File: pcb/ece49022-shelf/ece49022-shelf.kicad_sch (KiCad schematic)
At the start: 5 parts, among them J2 Conn_01x16_Pin, J3 Conn_01x04_Pin, J6 Conn_01x02_Pin, J7 Conn_01x02_Pin

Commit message: updated footprints, pcb
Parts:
- R11: footprint (none) -> Resistor_SMD:R_0402_1005Metric
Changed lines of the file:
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@@
 			)
 		)
-		(property "Footprint" ""
+		(property "Footprint" "Resistor_SMD:R_0402_1005Metric"
 			(at 179.07 105.41 0)
 			(effects

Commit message: stuff
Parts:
- added H1, H2, H3, H4: MountingHole, MountingHole:MountingHole_2.7mm_M2.5, symbol Mechanical:MountingHole
- R11: footprint Resistor_SMD:R_0402_1005Metric -> Resistor_SMD:R_0805_2012Metric_Pad1.20x1.40mm_HandSolder

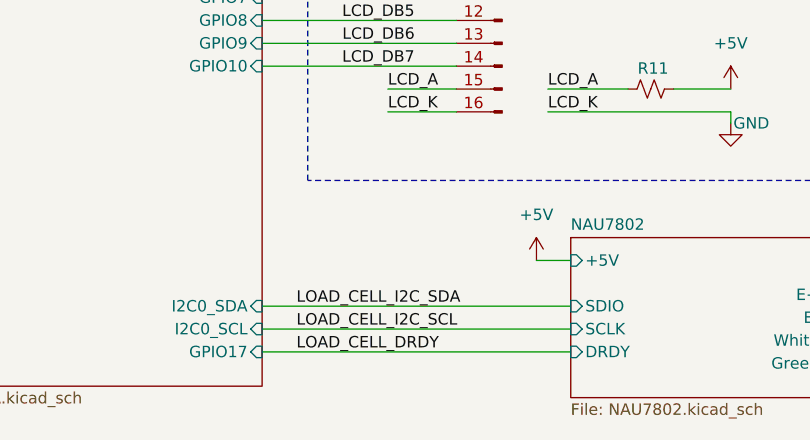
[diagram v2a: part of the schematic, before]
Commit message: edited nau7802 schem and changed pins for layout reasons
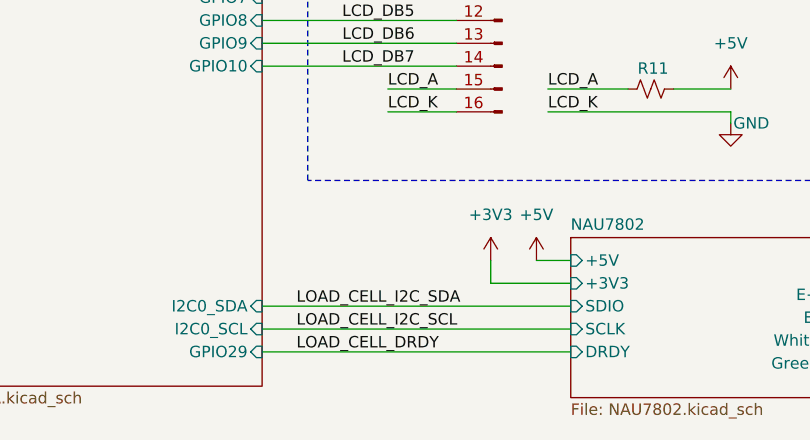
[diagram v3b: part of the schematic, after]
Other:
- sheet NAU7802 ports: added +3V3; removed none
- sheet RP2350A ports: added GPIO29; removed GPIO17
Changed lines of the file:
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@@
+	(wire
+		(pts
+			(xy 170.18 127) (xy 161.29 127)
+		)
+		(stroke
+			(width 0)
+			(type default)
+		)
+	)
 	(wire
 		(pts
@@
 		(pts
 			(xy 167.64 105.41) (xy 176.53 105.41)
+		)
+		(stroke
+			(width 0)
+			(type default)
+		)
+	)
+	(wire
+		(pts
+			(xy 161.29 124.46) (xy 161.29 127)
 		)
 		(stroke
@@
 	)
 	(symbol
+		(lib_id "power:+3V3")
+		(at 161.29 124.46 0)
+		(unit 1)
+		(exclude_from_sim no)
+		(in_bom yes)
+		(on_board yes)
+		(dnp no)
+		(fields_autoplaced yes)
+		(property "Reference" "#PWR02"
+			(at 161.29 128.27 0)
+			(effects
+				(font
+					(size 1.27 1.27)
+				)
+				(hide yes)
+			)
+		)
+		(property "Value" "+3V3"
+			(at 161.29 119.38 0)
+			(effects
+				(font
+					(size 1.27 1.27)
+				)
+			)
+		)
+		(property "Footprint" ""
+			(at 161.29 124.46 0)
+			(effects
+				(font
+					(size 1.27 1.27)
+				)
+				(hide yes)
+			)
+		)
+		(property "Datasheet" ""
+			(at 161.29 124.46 0)
+			(effects
+				(font
+					(size 1.27 1.27)
+				)
+				(hide yes)
+			)
+		)
+		(property "Description" "Power symbol creates a global label with name \"+3V3\""
+			(at 161.29 124.46 0)
+			(effects
+				(font
+					(size 1.27 1.27)
+				)
+				(hide yes)
+			)
+		)
+		(pin "1"
+		)
+		(instances
+			(project ""
+				(path "/cb6cb1b4-c151-4aa2-8cd7-5430288cfa02"
+					(reference "#PWR02")
+					(unit 1)
+				)
+			)
+		)
+	)
+	(symbol
 		(lib_id "Connector:Conn_01x02_Pin")
 		(at 35.56 129.54 0)
@@
 			)
 		)
-		(pin "GPIO17" input
-			(at 135.89 134.62 0)
-			(effects
-				(font
-					(size 1.27 1.27)
-				)
-				(justify right)
-			)
-		)
 		(pin "+3V3" input
 			(at 95.25 77.47 180)
@@
 				)
 				(justify left)
+			)
+		)
+		(pin "GPIO29" input
+			(at 135.89 134.62 0)
+			(effects
+				(font
+					(size 1.27 1.27)
+				)
+				(justify right)
 			)
 		)
@@
 			(effects
 				(font
+					(size 1.27 1.27)
+				)
+				(justify left)
+			)
+		)
+		(pin "+3V3" input
+			(at 170.18 127 180)
+			(effects
+				(font

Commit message: working on stuff
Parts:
- added RV1: R_Potentiometer_US, 49022_Footprints:RES_C01R00, symbol Device:R_Potentiometer_US
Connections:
- net +5V: now also RV1.1
- net GND: now also RV1.3
- net LCD_VO: now also RV1.2
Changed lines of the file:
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@@
 	(rectangle
 		(start 140.97 55.88)
-		(end 196.85 115.57)
+		(end 203.835 115.57)
 		(stroke
 			(width 0)
@@
 		)
 	)
+	(junction
+		(at 182.88 80.01)
+		(diameter 0)
+		(color 0 0 0 0)
+	)
+	(junction
+		(at 182.88 67.31)
+		(diameter 0)
+		(color 0 0 0 0)
+	)
 	(wire
 		(pts
@@
 	(wire
 		(pts
+			(xy 182.88 67.31) (xy 185.42 67.31)
+		)
+		(stroke
+			(width 0)
+			(type default)
+		)
+	)
+	(wire
+		(pts
 			(xy 135.89 132.08) (xy 170.18 132.08)
 		)
@@
 	(wire
 		(pts
+			(xy 185.42 77.47) (xy 185.42 80.01)
+		)
+		(stroke
+			(width 0)
+			(type default)
+		)
+	)
+	(wire
+		(pts
 			(xy 90.17 81.28) (xy 90.17 83.82)
 		)
@@
 	(wire
 		(pts
-			(xy 187.96 74.93) (xy 187.96 76.2)
+			(xy 182.88 80.01) (xy 182.88 81.28)
 		)
 		(stroke
@@
 	(wire
 		(pts
+			(xy 185.42 67.31) (xy 185.42 69.85)
+		)
+		(stroke
+			(width 0)
+			(type default)
+		)
+	)
+	(wire
+		(pts
 			(xy 99.06 40.64) (xy 99.06 41.91)
 		)
@@
 	(wire
 		(pts
-			(xy 177.8 69.85) (xy 187.96 69.85)
+			(xy 172.72 67.31) (xy 182.88 67.31)
 		)
 		(stroke
@@
 	(wire
 		(pts
-			(xy 187.96 67.31) (xy 187.96 69.85)
+			(xy 182.88 64.77) (xy 182.88 67.31)
 		)
 		(stroke
@@
 	(wire
 		(pts
+			(xy 189.23 73.66) (xy 199.39 73.66)
+		)
+		(stroke
+			(width 0)
+			(type default)
+		)
+	)
+	(wire
+		(pts
 			(xy 181.61 105.41) (xy 187.96 105.41)
 		)
@@
 	(wire
 		(pts
+			(xy 182.88 80.01) (xy 185.42 80.01)
+		)
+		(stroke
+			(width 0)
+			(type default)
+		)
+	)
+	(wire
+		(pts
 			(xy 48.26 118.11) (xy 48.26 119.38)
 		)
@@
 	(wire
 		(pts
-			(xy 177.8 74.93) (xy 187.96 74.93)
+			(xy 172.72 80.01) (xy 182.88 80.01)
 		)
 		(stroke
@@
 	)
 	(label "LCD_VSS"
-		(at 177.8 74.93 0)
+		(at 172.72 80.01 0)
 		(effects
 			(font
@@
 	)
 	(label "LCD_VDD"
-		(at 177.8 69.85 0)
+		(at 172.72 67.31 0)
 		(effects
 			(font
@@
 			)
 			(justify left bottom)
+		)
+	)
+	(label "LCD_VO"
+		(at 199.39 73.66 180)
+		(effects
+			(font
+				(size 1.27 1.27)
+			)
+			(justify right bottom)
 		)
 	)
@@
 	)
 	(symbol
+		(lib_id "Device:R_Potentiometer_US")
+		(at 185.42 73.66 0)
+		(unit 1)
+		(exclude_from_sim no)
+		(in_bom yes)
+		(on_board yes)
+		(dnp no)
+		(fields_autoplaced yes)
+		(property "Reference" "RV1"
+			(at 182.88 72.3899 0)
+			(effects
+				(font
+					(size 1.27 1.27)
+				)
+				(justify right)
+				(hide yes)
+			)
+		)
+		(property "Value" "R_Potentiometer_US"
+			(at 182.88 74.9299 0)
+			(effects
+				(font
+					(size 1.27 1.27)
+				)
+				(justify right)
+				(hide yes)
+			)
+		)
+		(property "Footprint" "49022_Footprints:RES_C01R00"
+			(at 185.42 73.66 0)
+			(effects
+				(font
+					(size 1.27 1.27)
+				)
+				(hide yes)
+			)
+		)
+		(property "Datasheet" "~"
+			(at 185.42 73.66 0)
+			(effects
+				(font
+					(size 1.27 1.27)
+				)
+				(hide yes)
+			)
+		)
+		(property "Description" "Potentiometer, US symbol"
+			(at 185.42 73.66 0)
+			(effects
+				(font
+					(size 1.27 1.27)
+				)
+				(hide yes)
+			)
+		)
+		(pin "3"
+		)
+		(pin "1"
+		)
+		(pin "2"
+		)
+		(instances
+			(project ""
+				(path "/cb6cb1b4-c151-4aa2-8cd7-5430288cfa02"
+					(reference "RV1")
+					(unit 1)
+				)
+			)
+		)
+	)
+	(symbol
 		(lib_id "power:+5V")
 		(at 105.41 40.64 0)
@@
 	(symbol
 		(lib_id "power:GND")
-		(at 187.96 76.2 0)
+		(at 182.88 81.28 0)
 		(unit 1)
 		(exclude_from_sim no)
@@
 		(fields_autoplaced yes)
 		(property "Reference" "#PWR049"
-			(at 187.96 82.55 0)
+			(at 182.88 87.63 0)
 			(effects
 				(font
@@
 		)
 		(property "Value" "GND"
-			(at 187.96 81.28 0)
+			(at 182.88 86.36 0)
 			(effects
 				(font
@@
 		)
 		(property "Footprint" ""
-			(at 187.96 76.2 0)
+			(at 182.88 81.28 0)
 			(effects
 				(font
@@
 		)
 		(property "Datasheet" ""
-			(at 187.96 76.2 0)
+			(at 182.88 81.28 0)
 			(effects
 				(font
@@
 		)
 		(property "Description" "Power symbol creates a global label with name \"GND\" , ground"
-			(at 187.96 76.2 0)
+			(at 182.88 81.28 0)
 			(effects
 				(font
@@
 	(symbol
 		(lib_id "power:+5V")
-		(at 187.96 67.31 0)
+		(at 182.88 64.77 0)
 		(unit 1)
 		(exclude_from_sim no)
@@
 		(fields_autoplaced yes)
 		(property "Reference" "#PWR050"
-			(at 187.96 71.12 0)
+			(at 182.88 68.58 0)
 			(effects
 				(font
@@
 		)
 		(property "Value" "+5V"
-			(at 187.96 62.23 0)
+			(at 182.88 59.69 0)
 			(effects
 				(font
@@
 		)
 		(property "Footprint" ""
-			(at 187.96 67.31 0)
+			(at 182.88 64.77 0)
 			(effects
 				(font
@@
 		)
 		(property "Datasheet" ""
-			(at 187.96 67.31 0)
+			(at 182.88 64.77 0)
 			(effects
 				(font
@@
 		)
 		(property "Description" "Power symbol creates a global label with name \"+5V\""
-			(at 187.96 67.31 0)
-			(effects
-				(font
+			(at 182.88 64.77 0)
+			(effects
+				(font

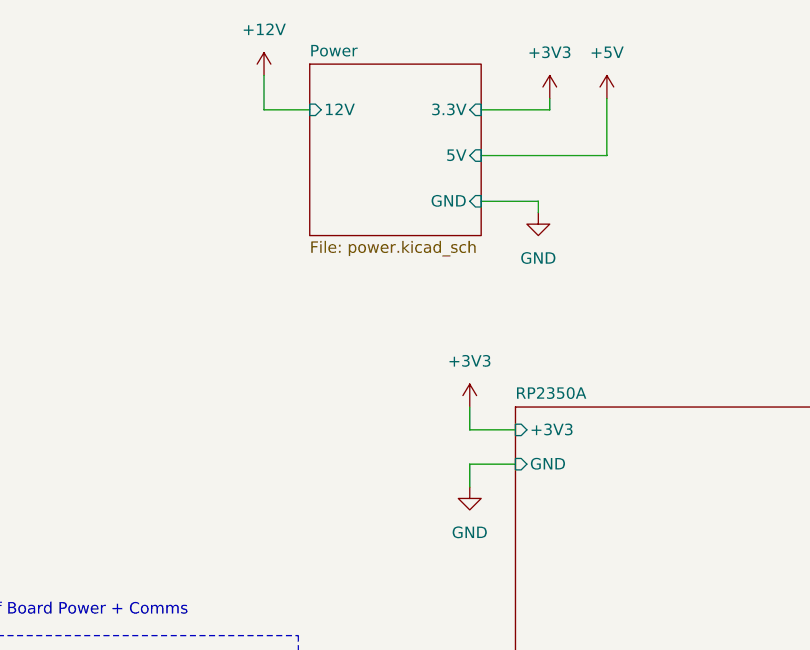
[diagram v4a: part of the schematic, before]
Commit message: new converter layout
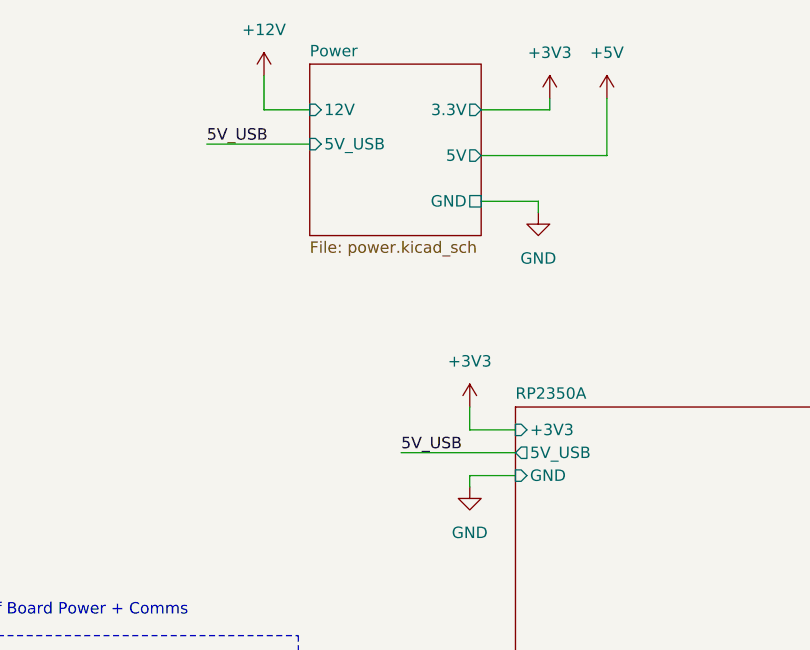
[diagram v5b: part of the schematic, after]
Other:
- sheet Power ports: added 5V_USB; removed none
- sheet RP2350A ports: added 5V_USB; removed none
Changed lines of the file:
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@@
 	(wire
 		(pts
-			(xy 90.17 81.28) (xy 90.17 83.82)
+			(xy 90.17 82.55) (xy 90.17 83.82)
 		)
 		(stroke
@@
 	(wire
 		(pts
+			(xy 60.96 45.72) (xy 72.39 45.72)
+		)
+		(stroke
+			(width 0)
+			(type default)
+		)
+	)
+	(wire
+		(pts
 			(xy 135.89 134.62) (xy 170.18 134.62)
 		)
@@
 	(wire
 		(pts
-			(xy 95.25 81.28) (xy 90.17 81.28)
+			(xy 95.25 82.55) (xy 90.17 82.55)
 		)
 		(stroke
@@
 		(pts
 			(xy 182.88 80.01) (xy 185.42 80.01)
+		)
+		(stroke
+			(width 0)
+			(type default)
+		)
+	)
+	(wire
+		(pts
+			(xy 82.55 80.01) (xy 95.25 80.01)
 		)
 		(stroke
@@
 		)
 	)
+	(label "5V_USB"
+		(at 82.55 80.01 0)
+		(effects
+			(font
+				(size 1.27 1.27)
+			)
+			(justify left bottom)
+		)
+	)
 	(label "LCD_DB1"
 		(at 144.78 87.63 0)
@@
 	(label "LCD_K"
 		(at 149.86 107.95 0)
+		(effects
+			(font
+				(size 1.27 1.27)
+			)
+			(justify left bottom)
+		)
+	)
+	(label "5V_USB"
+		(at 60.96 45.72 0)
 		(effects
 			(font
@@
 			)
 		)
-		(pin "5V" input
-			(at 91.44 46.99 0)
-			(effects
-				(font
-					(size 1.27 1.27)
-				)
-				(justify right)
-			)
-		)
-		(pin "3.3V" input
-			(at 91.44 41.91 0)
-			(effects
-				(font
-					(size 1.27 1.27)
-				)
-				(justify right)
-			)
-		)
 		(pin "12V" input
 			(at 72.39 41.91 180)
@@
 			)
 		)
-		(pin "GND" input
+		(pin "5V_USB" input
+			(at 72.39 45.72 180)
+			(effects
+				(font
+					(size 1.27 1.27)
+				)
+				(justify left)
+			)
+		)
+		(pin "5V" output
+			(at 91.44 46.99 0)
+			(effects
+				(font
+					(size 1.27 1.27)
+				)
+				(justify right)
+			)
+		)
+		(pin "3.3V" output
+			(at 91.44 41.91 0)
+			(effects
+				(font
+					(size 1.27 1.27)
+				)
+				(justify right)
+			)
+		)
+		(pin "GND" passive
 			(at 91.44 52.07 0)
 			(effects
@@
 		)
 		(pin "GND" input
-			(at 95.25 81.28 180)
+			(at 95.25 82.55 180)
 			(effects
 				(font
@@
 			)
 		)
+		(pin "5V_USB" output
+			(at 95.25 80.01 180)
+			(effects
+				(font
+					(size 1.27 1.27)
+				)
+				(justify left)
+			)
+		)

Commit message: stuff
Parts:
- added J5: Conn_02x03_Counter_Clockwise, Connector_PinHeader_2.54mm:PinHeader_2x03_P2.54mm_Vertical, symbol Connector_Generic:Conn_02x03_Counter_Clockwise
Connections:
- new net GPIO_AUX_16: J5.1 (Pin_1)
- new net GPIO_AUX_17: J5.2 (Pin_2)
- new net GPIO_AUX_18: J5.3 (Pin_3)
- new net GPIO_AUX_19: J5.6 (Pin_6)
- new net GPIO_AUX_20: J5.5 (Pin_5)
- new net GPIO_AUX_21: J5.4 (Pin_4)
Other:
- sheet RP2350A ports: added GPIO16, GPIO17, GPIO18, GPIO19, GPIO20, GPIO21; removed none
- moved on the sheet: J6, J7

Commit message: layout chanes
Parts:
- removed J6: Conn_01x02_Pin, Connector_PinHeader_2.54mm:PinHeader_1x02_P2.54mm_Vertical, symbol Connector:Conn_01x02_Pin
- added J6: Conn_01x03_Pin, Connector_PinHeader_1.00mm:PinHeader_1x03_P1.00mm_Vertical, symbol Connector:Conn_01x03_Pin
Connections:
- net GND: now also J6.3 (Pin_3)
- net GPIO_AUX_16: now also J5.5 (Pin_5); no longer J5.1 (Pin_1)
- net GPIO_AUX_17: now also J5.3 (Pin_3); no longer J5.2 (Pin_2)
- net GPIO_AUX_18: now also J5.1 (Pin_1); no longer J5.3 (Pin_3)
- net GPIO_AUX_19: now also J5.2 (Pin_2); no longer J5.6 (Pin_6)
- net GPIO_AUX_20: now also J5.4 (Pin_4); no longer J5.5 (Pin_5)
- net GPIO_AUX_21: now also J5.6 (Pin_6); no longer J5.4 (Pin_4)
- net MAIN_MCU_I2C_SCL: now also J6.2 (Pin_2)
- net MAIN_MCU_I2C_SDA: now also J6.1 (Pin_1)
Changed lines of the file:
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@@
 	(rectangle
 		(start 26.67 116.205)
-		(end 68.58 144.78)
+		(end 68.58 149.225)
 		(stroke
 			(width 0)
@@
 	(wire
 		(pts
+			(xy 38.1 144.78) (xy 43.18 144.78)
+		)
+		(stroke
+			(width 0)
+			(type default)
+		)
+	)
+	(wire
+		(pts
 			(xy 72.39 41.91) (xy 67.31 41.91)
 		)
@@
 		)
 	)
-	(label "GPIO_AUX_20"
-		(at 63.5 101.6 180)
-		(effects
-			(font
-				(size 1.27 1.27)
-			)
-			(justify right bottom)
-		)
-	)
 	(label "MAIN_MCU_I2C_SCL"
 		(at 58.42 142.24 180)
@@
 		)
 	)
-	(label "GPIO_AUX_19"
-		(at 63.5 99.06 180)
-		(effects
-			(font
-				(size 1.27 1.27)
-			)
-			(justify right bottom)
+	(label "GPIO_AUX_17"
+		(at 22.86 104.14 0)
+		(effects
+			(font
+				(size 1.27 1.27)
+			)
+			(justify left bottom)
 		)
 	)
@@
 		)
 	)
-	(label "GPIO_AUX_17"
-		(at 22.86 101.6 0)
-		(effects
-			(font
-				(size 1.27 1.27)
-			)
-			(justify left bottom)
-		)
-	)
 	(label "LOAD_CELL_DRDY"
 		(at 139.7 134.62 0)
@@
 		)
 	)
+	(label "GPIO_AUX_20"
+		(at 63.5 104.14 180)
+		(effects
+			(font
+				(size 1.27 1.27)
+			)
+			(justify right bottom)
+		)
+	)
 	(label "LOAD_CELL_I2C_SCL"
 		(at 139.7 132.08 0)
@@
 		)
 	)
-	(label "GPIO_AUX_21"
-		(at 63.5 104.14 180)
-		(effects
-			(font
-				(size 1.27 1.27)
-			)
-			(justify right bottom)
-		)
-	)
-	(label "GPIO_AUX_16"
-		(at 22.86 99.06 0)
-		(effects
-			(font
-				(size 1.27 1.27)
-			)
-			(justify left bottom)
-		)
-	)
 	(label "GPIO_AUX_18"
 		(at 77.47 102.87 0)
@@
 		)
 	)
+	(label "GPIO_AUX_16"
+		(at 63.5 101.6 180)
+		(effects
+			(font
+				(size 1.27 1.27)
+			)
+			(justify right bottom)
+		)
+	)
 	(label "GPIO_AUX_21"
 		(at 77.47 110.49 0)
@@
 		)
 	)
+	(label "GPIO_AUX_19"
+		(at 22.86 101.6 0)
+		(effects
+			(font
+				(size 1.27 1.27)
+			)
+			(justify left bottom)
+		)
+	)
 	(label "MAIN_MCU_I2C_SDA"
 		(at 58.42 139.7 180)
@@
 	)
 	(label "GPIO_AUX_18"
-		(at 22.86 104.14 0)
-		(effects
-			(font
-				(size 1.27 1.27)
-			)
-			(justify left bottom)
+		(at 22.86 99.06 0)
+		(effects
+			(font
+				(size 1.27 1.27)
+			)
+			(justify left bottom)
+		)
+	)
+	(label "GPIO_AUX_21"
+		(at 63.5 99.06 180)
+		(effects
+			(font
+				(size 1.27 1.27)
+			)
+			(justify right bottom)
 		)
 	)
@@
 	(symbol
 		(lib_id "Connector:Conn_01x02_Pin")
-		(at 33.02 139.7 0)
-		(unit 1)
-		(exclude_from_sim no)
-		(in_bom yes)
-		(on_board yes)
-		(dnp no)
-		(property "Reference" "J6"
-			(at 33.528 136.652 0)
-			(effects
-				(font
-					(size 1.27 1.27)
-				)
-			)
-		)
-		(property "Value" "Conn_01x02_Pin"
-			(at 33.655 137.16 0)
-			(effects
-				(font
-					(size 1.27 1.27)
-				)
-				(hide yes)
-			)
-		)
-		(property "Footprint" "Connector_PinHeader_2.54mm:PinHeader_1x02_P2.54mm_Vertical"
-			(at 33.02 139.7 0)
-			(effects
-				(font
-					(size 1.27 1.27)
-				)
-				(hide yes)
-			)
-		)
-		(property "Datasheet" "~"
-			(at 33.02 139.7 0)
-			(effects
-				(font
-					(size 1.27 1.27)
-				)
-				(hide yes)
-			)
-		)
-		(property "Description" "Generic connector, single row, 01x02, script generated"
-			(at 33.02 139.7 0)
-			(effects
-				(font
-					(size 1.27 1.27)
-				)
-				(hide yes)
-			)
-		)
-		(pin "2"
-		)
-		(pin "1"
-		)
-		(instances
-			(project "ece49022-shelf"
-				(path "/cb6cb1b4-c151-4aa2-8cd7-5430288cfa02"
-					(reference "J6")
-					(unit 1)
-				)
-			)
-		)
-	)
-	(symbol
-		(lib_id "Connector:Conn_01x02_Pin")
 		(at 33.02 125.73 0)
 		(unit 1)
@@
 				(path "/cb6cb1b4-c151-4aa2-8cd7-5430288cfa02"
 					(reference "#PWR052")
+					(unit 1)
+				)
+			)
+		)
+	)
+	(symbol
+		(lib_id "power:GND")
+		(at 43.18 144.78 0)
+		(unit 1)
+		(exclude_from_sim no)
+		(in_bom yes)
+		(on_board yes)
+		(dnp no)
+		(property "Reference" "#PWR057"
+			(at 43.18 151.13 0)
+			(effects
+				(font
+					(size 1.27 1.27)
+				)
+				(hide yes)
+			)
+		)
+		(property "Value" "GND"
+			(at 45.974 145.034 0)
+			(effects
+				(font
+					(size 1.27 1.27)
+				)
+			)
+		)
+		(property "Footprint" ""
+			(at 43.18 144.78 0)
+			(effects
+				(font
+					(size 1.27 1.27)
+				)
+				(hide yes)
+			)
+		)
+		(property "Datasheet" ""
+			(at 43.18 144.78 0)
+			(effects
+				(font
+					(size 1.27 1.27)
+				)
+				(hide yes)
+			)
+		)
+		(property "Description" "Power symbol creates a global label with name \"GND\" , ground"
+			(at 43.18 144.78 0)
+			(effects
+				(font
+					(size 1.27 1.27)
+				)
+				(hide yes)
+			)
+		)
+		(pin "1"
+		)
+		(instances
+			(project "ece49022-shelf"
+				(path "/cb6cb1b4-c151-4aa2-8cd7-5430288cfa02"
+					(reference "#PWR057")
 					(unit 1)
 				)
@@
 					(unit 1)
 				)
+			)
+		)
+	)
+	(symbol
+		(lib_id "Connector:Conn_01x03_Pin")
+		(at 33.02 142.24 0)
+		(unit 1)
+		(exclude_from_sim no)
+		(in_bom yes)
+		(on_board yes)
+		(dnp no)
+		(property "Reference" "J6"
+			(at 35.56 134.62 0)
+			(effects
+				(font
+					(size 1.27 1.27)
+				)
+			)
+		)
+		(property "Value" "Conn_01x03_Pin"
+			(at 36.068 136.906 0)
+			(effects
+				(font
+					(size 1.27 1.27)
+				)
+			)
+		)
+		(property "Footprint" "Connector_PinHeader_1.00mm:PinHeader_1x03_P1.00mm_Vertical"
+			(at 33.02 142.24 0)
+			(effects
+				(font
+					(size 1.27 1.27)
+				)
+				(hide yes)
+			)
+		)
+		(property "Datasheet" "~"
+			(at 33.02 142.24 0)
+			(effects
+				(font
+					(size 1.27 1.27)
+				)
+				(hide yes)
+			)
+		)
+		(property "Description" "Generic connector, single row, 01x03, script generated"
+			(at 33.02 142.24 0)
+			(effects
+				(font
+					(size 1.27 1.27)
+				)
+				(hide yes)
+			)
+		)
+		(pin "3"
+		)
+		(pin "1"
+		)
+		(pin "2"
+		)
+		(instances
+			(project ""
+				(path "/cb6cb1b4-c151-4aa2-8cd7-5430288cfa02"
+					(reference "J6")
+					(unit 1)
+				)

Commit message: stuff
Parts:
- added D2: D_Schottky, 49022_Footprints:SMFDO-219AB_VIS-L, symbol Device:D_Schottky
- added J8: Conn_02x03_Counter_Clockwise, Connector_PinHeader_2.54mm:PinHeader_2x03_P2.54mm_Vertical, symbol Connector_Generic:Conn_02x03_Counter_Clockwise
- added R20: 100, Resistor_SMD:R_0603_1608Metric, symbol Device:R_Small_US
- J6: footprint Connector_PinHeader_1.00mm:PinHeader_1x03_P1.00mm_Vertical -> Connector_PinHeader_2.54mm:PinHeader_1x03_P2.54mm_Vertical
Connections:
- net +12V: now also D2.1 (K); no longer J7.1 (Pin_1)
- net GND: now also J8.1 (Pin_1), J8.2 (Pin_2), J8.3 (Pin_3), J8.4 (Pin_4), J8.5 (Pin_5), J8.6 (Pin_6)
- net GPIO_AUX_21 renamed LED
- net LED: now also R20.1
- new net: D2.2 (A), J7.1 (Pin_1)
- new net RP2350A/GPIO21: R20.2
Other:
- moved on the sheet: J5
